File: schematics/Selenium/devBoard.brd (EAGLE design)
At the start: 33.8 x 23.6 mm, 21 parts, among them J2 629105136821, U1 TSL2591, U5 MCP73831SOT23-5

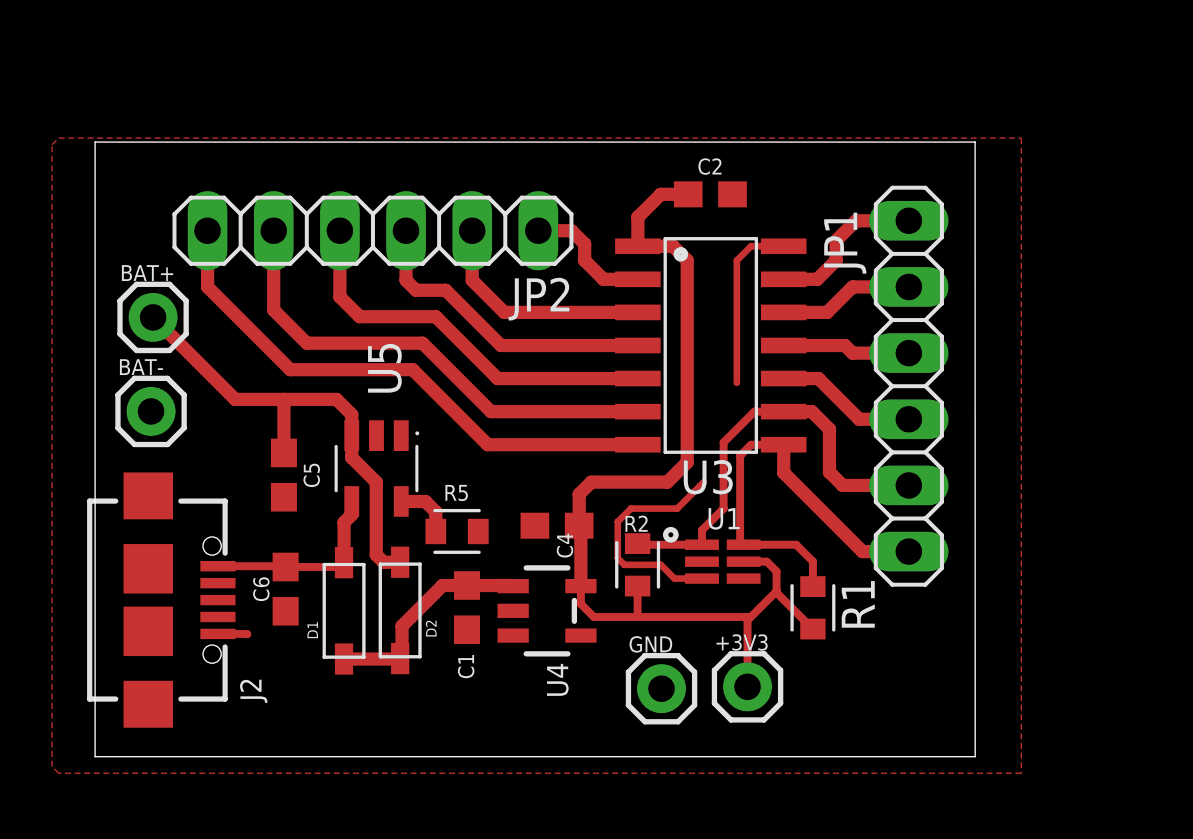
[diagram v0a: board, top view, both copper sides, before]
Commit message: Add enable pin pads for regulator, tidy, then untrack backup files
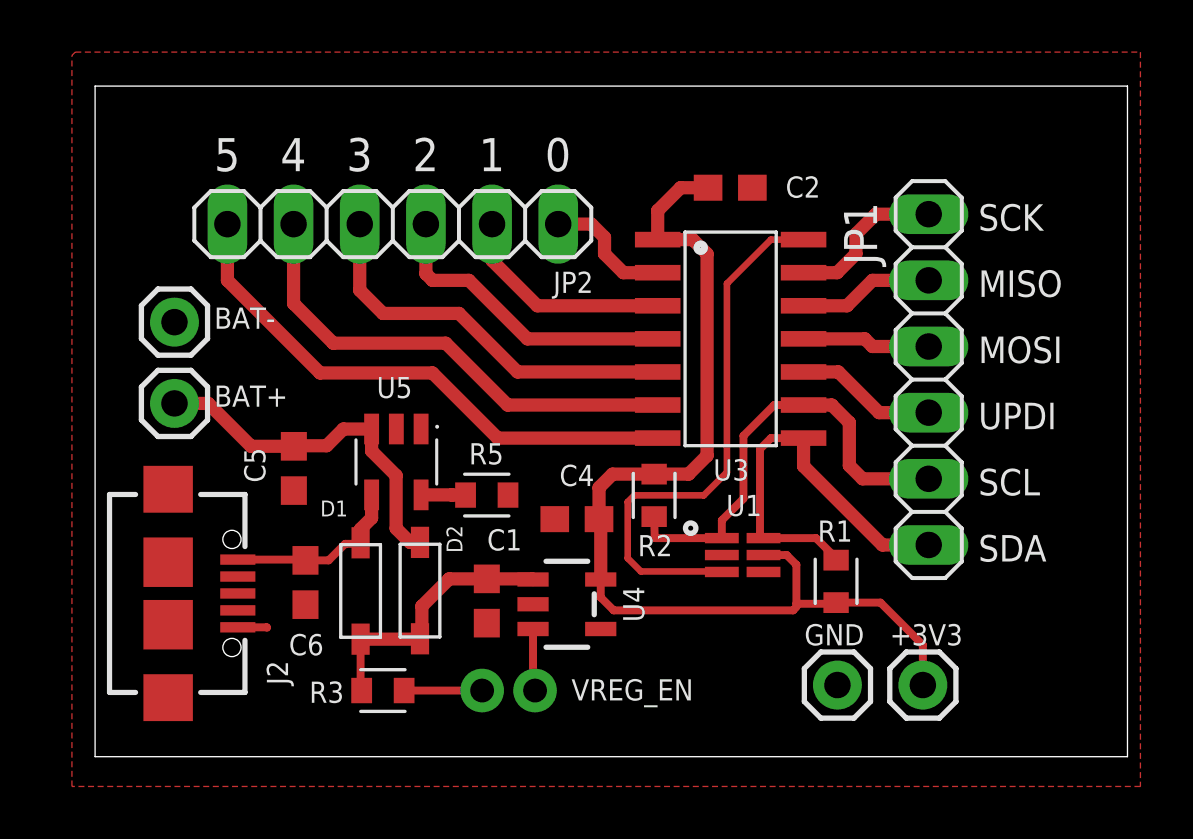
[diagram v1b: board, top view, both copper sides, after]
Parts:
- added R3: 100K, Resistor:RESC1608X60
- added TP2, VREG_EN: TESTPOINT_TPS-PAD-036, 52101-101-REV-A_v16:TESTPOINT_PAD-036
- D1, D2: value (none) -> MBR120
- moved GND 6.76 mm to (28.5, 2.75)
- moved +3V3 6.73 mm to (31.8, 2.75)
- moved BAT- 3.54 mm to (3.05, 16.7)
- moved BAT+ 3.40 mm to (3.05, 13.6)
- moved R2 2.74 mm to (21.5, 10.0), turned to 270 degrees
- moved R5 1.81 mm to (15.0, 10.0)
- moved R1 1.35 mm to (28.4, 6.73)
- moved D2 1.08 mm to (12.5, 6.38)
- moved D1 0.99 mm to (10.2, 6.36)
- moved C2 0.80 mm to (24.4, 21.8)
- moved U5 0.80 mm to (11.6, 11.3)
- moved U4 0.80 mm to (18.1, 5.85)
- moved C4 0.80 mm to (18.5, 9.12)
- moved J2 0.80 mm to (3.15, 6.27)
- moved C6 0.80 mm to (8.08, 6.69)
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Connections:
- new net N$13: R3.1, VREG_EN.1
- new net N$14: TP2.1, U4.3
- net N$1: now also R3.2
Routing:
- net GND: track 16.7 -> 22.3 mm
- net VBAT: track 19.0 -> 14.2 mm
- net N$13: track 0.00 -> 2.99 mm
- net N$14: track 0.00 -> 2.39 mm
- net N$1: track 8.42 -> 10.7 mm
- net 3V3: track 38.4 -> 40.0 mm
- net SCL_3V: track 16.5 -> 17.4 mm
- net SDA_3V: track 16.3 -> 15.6 mm
- net N$4: track 2.33 -> 1.79 mm
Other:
- board size 33.8 x 23.6 mm -> 39.6 x 25.7 mm
- board text added: "0"
- board text added: "1"
- board text added: "2"
- board text added: "3"
- board text added: "4"
- board text added: "5"
- board text added: "MISO"
- board text added: "MOSI"
- board text added: "SCK"
- board text added: "SCL"
- board text added: "SDA"
- board text added: "UPDI"
